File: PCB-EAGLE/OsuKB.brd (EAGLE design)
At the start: 50 x 50 mm, 72 parts, among them X1 USB-MINIB-5PIN

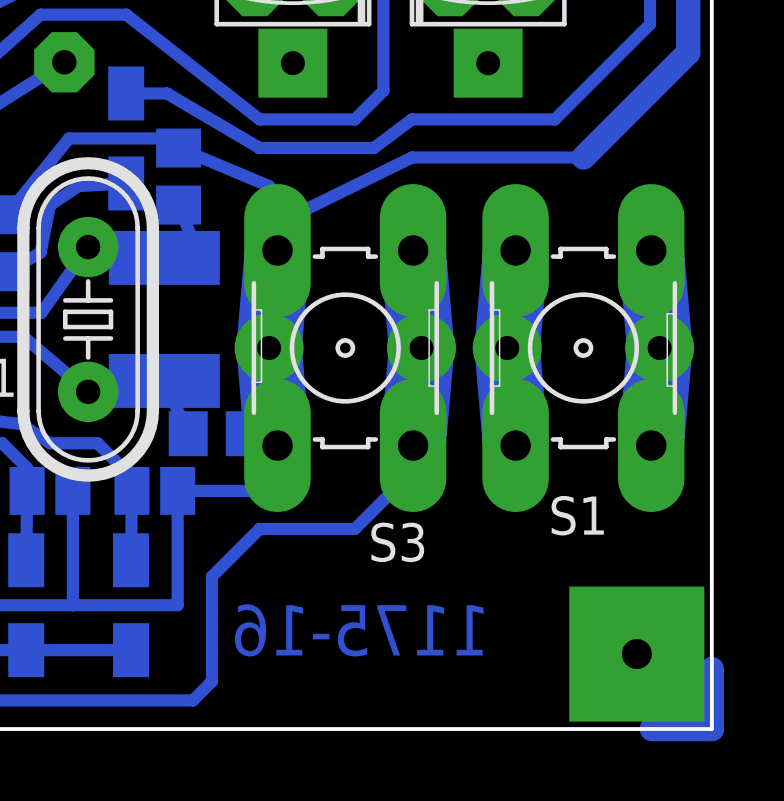
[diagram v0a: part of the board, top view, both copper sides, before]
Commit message: move esc
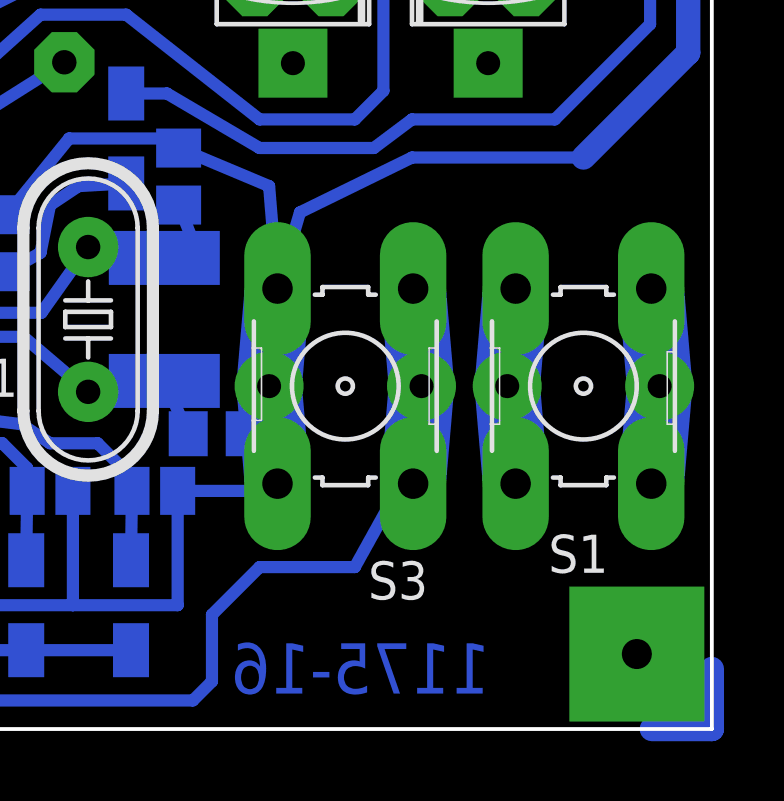
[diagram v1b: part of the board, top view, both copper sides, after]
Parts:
- moved S1 1.27 mm to (59.7, 31.8)
- moved S3 1.27 mm to (51.8, 31.8)
- moved U$1 1.27 mm to (59.7, 32.4)
- moved U$6 1.27 mm to (51.8, 31.1)
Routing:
- net GND: track 235.7 -> 237.7 mm
- net S3: track 68.7 -> 67.6 mm

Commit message: ed sh na
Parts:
- R10: value (none) -> 10k
- R13, R14: value (none) -> 1k
- S1.1, S2.1: value MP5 -> MP9R-1
- S1.2, S2.2: value MP5 -> (none)
- VD1, VD2: value (none) -> 3v6
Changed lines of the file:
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@@
 <attribute name="VALUE" x="32.385" y="57.785" size="1.27" layer="28" rot="MR90"/>
 </element>
-<element name="VD1" library="diode" package="DO34Z7" value="" x="46.0375" y="62.5475" smashed="yes" rot="R90">
+<element name="VD1" library="diode" package="DO34Z7" value="3v6" x="46.0375" y="62.5475" smashed="yes" rot="R90">
 <attribute name="NAME" x="49.4665" y="69.6595" size="1.27" layer="25" ratio="10" rot="R180"/>
 <attribute name="VALUE" x="48.4505" y="61.0235" size="1.27" layer="27" ratio="10" rot="R90"/>
 </element>
-<element name="VD2" library="diode" package="DO34Z7" value="" x="32.0675" y="60.96" smashed="yes" rot="R90">
+<element name="VD2" library="diode" package="DO34Z7" value="3v6" x="32.0675" y="60.96" smashed="yes" rot="R90">
 <attribute name="NAME" x="32.3215" y="69.6595" size="1.27" layer="25" ratio="10" rot="R180"/>
 <attribute name="VALUE" x="34.4805" y="59.436" size="1.27" layer="27" ratio="10" rot="R90"/>
@@
 <attribute name="VALUE" x="48.73625" y="40.005" size="1.27" layer="28" rot="MR270"/>
 </element>
-<element name="R10" library="rcl" package="R1206W" value="" x="21.59" y="28.575" smashed="yes" rot="MR180">
+<element name="R10" library="rcl" package="R1206W" value="10k" x="21.59" y="28.575" smashed="yes" rot="MR180">
 <attribute name="NAME" x="20.0025" y="26.9875" size="1.27" layer="26" rot="MR180"/>
 <attribute name="VALUE" x="19.685" y="31.115" size="1.27" layer="28" rot="MR180"/>
@@
 <element name="U$6" library="osukb" package="PROGRAMMER_KEY" value="PROGRAMMER_5.08" x="51.7525" y="31.115"/>
 <element name="GND" library="osukb" package="KB2" value="KB2" x="13.97" y="20.32"/>
-<element name="S1.1" library="osukb" package="MP5" value="MP5" x="50.00625" y="56.515"/>
-<element name="S1.2" library="osukb" package="MP5" value="MP5" x="56.515" y="56.515"/>
-<element name="S2.1" library="osukb" package="MP5" value="MP5" x="28.09875" y="56.515"/>
-<element name="S2.2" library="osukb" package="MP5" value="MP5" x="21.59" y="56.515"/>
+<element name="S1.1" library="osukb" package="MP5" value="MP9R-1" x="50.00625" y="56.515"/>
+<element name="S1.2" library="osukb" package="MP5" value="" x="56.515" y="56.515"/>
+<element name="S2.1" library="osukb" package="MP5" value="MP9R-1" x="28.09875" y="56.515"/>
+<element name="S2.2" library="osukb" package="MP5" value="" x="21.59" y="56.515"/>
 <element name="ZS" library="rcl" package="C1812K" value="" x="45.72" y="33.9725" smashed="yes" rot="MR270">
 <attribute name="NAME" x="45.747503125" y="37.509996875" size="1.016" layer="26" rot="MR0"/>
@@
 <attribute name="VALUE" x="19.685" y="46.736" size="1.27" layer="27" ratio="10" rot="R180"/>
 </element>
-<element name="R13" library="osukb" package="R1206W" value="" x="60.325" y="53.6575" smashed="yes" rot="MR270">
+<element name="R13" library="osukb" package="R1206W" value="1k" x="60.325" y="53.6575" smashed="yes" rot="MR270">
 <attribute name="NAME" x="58.1025" y="51.1175" size="1.27" layer="26" rot="MR90"/>
 <attribute name="VALUE" x="62.865" y="55.5625" size="1.27" layer="28" rot="MR270"/>
 </element>
-<element name="R14" library="rcl" package="0207/12" value="" x="36.03625" y="42.545" smashed="yes" rot="MR180">
+<element name="R14" library="rcl" package="0207/12" value="1k" x="36.03625" y="42.545" smashed="yes" rot="MR180">
 <attribute name="NAME" x="34.44875" y="43.053" size="1.27" layer="26" ratio="10" rot="MR180"/>
 <attribute name="VALUE" x="33.75025" y="43.2308" size="1.27" layer="28" ratio="10" rot="MR180"/>
